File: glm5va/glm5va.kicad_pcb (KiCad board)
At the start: 2 copper layers, 21 parts, among them J1 BANK_xx1, J2 JIN, J3 POWER, U1 74HC245, U2 74HC245

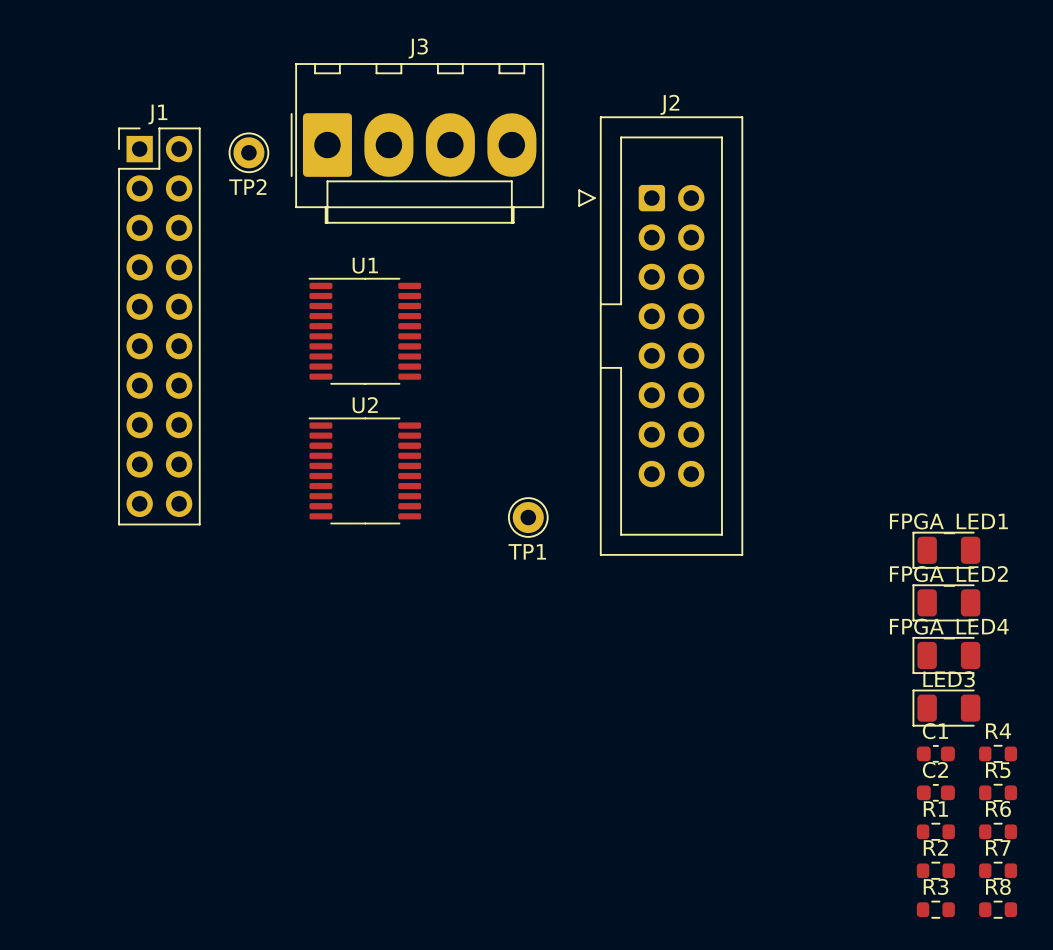
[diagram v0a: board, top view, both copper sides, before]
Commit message: glm5va: place components
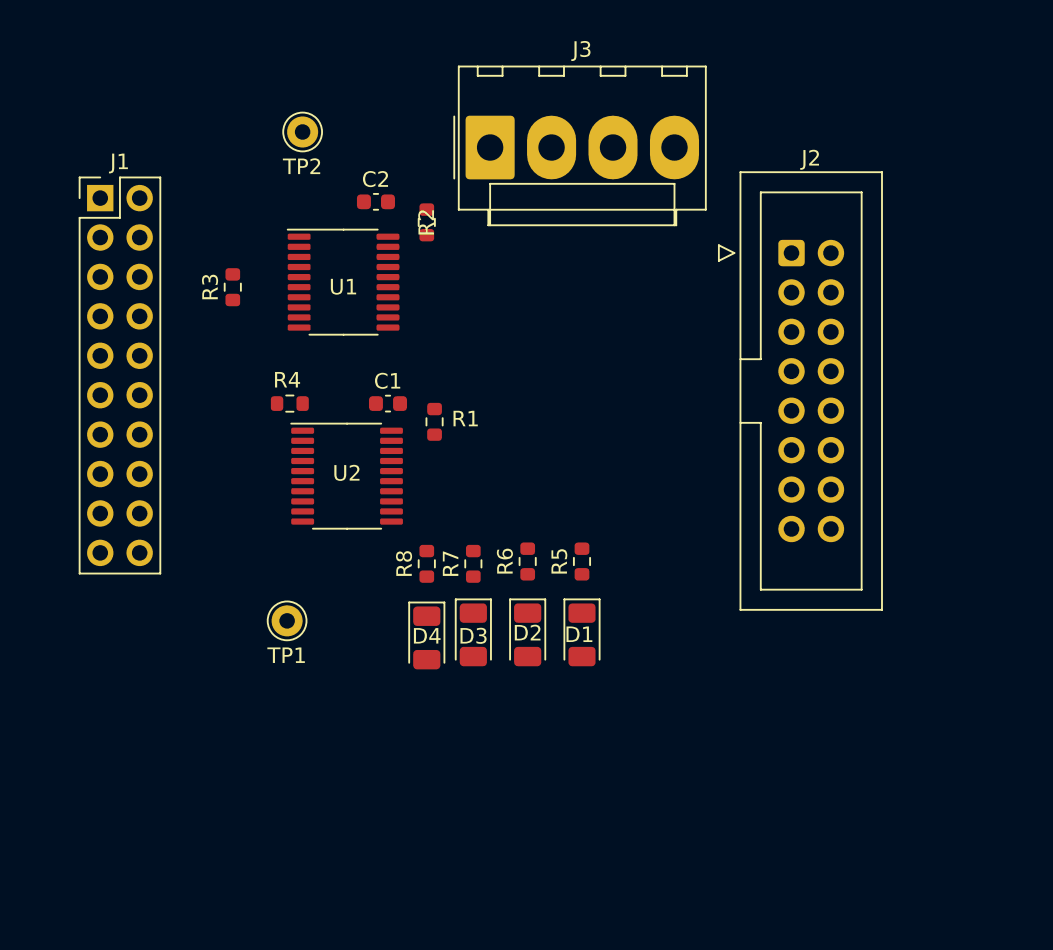
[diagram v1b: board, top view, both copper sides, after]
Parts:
- removed FPGA_LED1, FPGA_LED2, FPGA_LED4, LED3: 0603, LED_SMD:LED_1206_3216Metric
- added D1: 0603, LED_SMD:LED_1206_3216Metric, F.Cu at (151.0, 101.9)
- added D2: 0603, LED_SMD:LED_1206_3216Metric, F.Cu at (147.5, 101.9)
- added D3: 0603, LED_SMD:LED_1206_3216Metric, F.Cu at (144.0, 101.9)
- added D4: 0603, LED_SMD:LED_1206_3216Metric, F.Cu at (141.0, 102.1)
- R5, R6, R7, R8: value 2.2k/R0402 -> 2.2k
- moved R3 60.5 mm to (128.5, 79.5), turned to 90 degrees
- moved R2 53.1 mm to (141.0, 75.3), turned to 90 degrees
- moved C2 52.5 mm to (137.7, 74.0)
- moved R4 50.9 mm to (132.2, 87.0), turned to 180 degrees
- moved R8 43.0 mm to (141.0, 97.3), turned to 90 degrees
- moved C1 41.9 mm to (138.5, 87.0)
- moved R1 41.7 mm to (141.5, 88.2), turned to 90 degrees
- moved R7 39.2 mm to (144.0, 97.3), turned to 90 degrees
- moved R6 35.0 mm to (147.5, 97.2), turned to 90 degrees
- moved R5 30.7 mm to (151.0, 97.2), turned to 90 degrees
- moved TP1 16.9 mm to (132.0, 101.0)
- moved J3 10.5 mm to (145.1, 70.5)
- moved J2 9.67 mm to (164.5, 77.3)
- moved J1 4.05 mm to (120.0, 73.8)
- moved TP2 3.71 mm to (133.0, 69.5)
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
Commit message: glm5va: routing and layers ok
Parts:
- added G***: LOGO, LOGO, B.Cu at (136.0, 85.0)
- moved D4 11.2 mm to (151.0, 97.1)
- moved D3 11.1 mm to (154.0, 97.1)
- moved R7 11.0 mm to (154.0, 92.7)
- moved R8 11.0 mm to (151.0, 92.7)
- moved D2 10.6 mm to (157.0, 97.1)
- moved R6 10.5 mm to (157.0, 92.7)
- moved D1 10.2 mm to (160.0, 97.1)
- moved R5 10.1 mm to (160.0, 92.7)
- moved R3 7.66 mm to (133.8, 74.0), turned to 180 degrees
- moved J3 6.42 mm to (147.1, 76.6)
- moved TP2 5.41 mm to (128.5, 72.5)
- moved TP1 4.61 mm to (128.5, 98.0)
- moved J2 2.50 mm to (167.0, 76.9)
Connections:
- J1 pad 10: Net-(J1-Pin_10) -> /BANK_B5
- J1 pad 11: Net-(J1-Pin_11) -> /BANK_A4
- J1 pad 12: Net-(J1-Pin_12) -> /BANK_B4
- J1 pad 13: Net-(J1-Pin_13) -> /BANK_A3
- J1 pad 14: Net-(J1-Pin_14) -> /BANK_B3
- J1 pad 15: Net-(J1-Pin_15) -> /BANK_A2
- J1 pad 16: Net-(J1-Pin_16) -> /BANK_B2
- J1 pad 17: Net-(J1-Pin_17) -> /BANK_A1
- J1 pad 18: Net-(J1-Pin_18) -> /BANK_B1
- J1 pad 3: Net-(J1-Pin_3) -> /BANK_A8
- J1 pad 4: Net-(J1-Pin_4) -> /BANK_B8
- J1 pad 5: Net-(J1-Pin_5) -> /BANK_A7
- J1 pad 6: Net-(J1-Pin_6) -> /BANK_B7
- J1 pad 7: Net-(J1-Pin_7) -> /BANK_A6
- J1 pad 8: Net-(J1-Pin_8) -> /BANK_B6
- J1 pad 9: Net-(J1-Pin_9) -> /BANK_A5
- U1 pad 2: Net-(J1-Pin_17) -> /BANK_A8
- U1 pad 3: Net-(J1-Pin_15) -> /BANK_B8
- U1 pad 4: Net-(J1-Pin_13) -> /BANK_A7
- U1 pad 5: Net-(J1-Pin_11) -> /BANK_B7
- U1 pad 6: Net-(J1-Pin_9) -> /BANK_A6
- U1 pad 7: Net-(J1-Pin_7) -> /BANK_B6
- U1 pad 8: Net-(J1-Pin_5) -> /BANK_A5
- U1 pad 9: Net-(J1-Pin_3) -> /BANK_B5
- U2 pad 2: Net-(J1-Pin_18) -> /BANK_A4
- U2 pad 3: Net-(J1-Pin_16) -> /BANK_B4
- U2 pad 4: Net-(J1-Pin_14) -> /BANK_A3
- U2 pad 5: Net-(J1-Pin_12) -> /BANK_B3
- U2 pad 6: Net-(J1-Pin_10) -> /BANK_A2
- U2 pad 7: Net-(J1-Pin_8) -> /BANK_B2
- U2 pad 8: Net-(J1-Pin_6) -> /BANK_A1
- U2 pad 9: Net-(J1-Pin_4) -> /BANK_B1
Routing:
- net /B: track 0.00 -> 43.9 mm
- net /LAT: track 0.00 -> 40.2 mm
- net /G1: track 0.00 -> 37.8 mm, vias 0 -> 2
- net /G2: track 0.00 -> 34.7 mm, vias 0 -> 2
- net /OE: track 0.00 -> 33.7 mm
- net /CLK: track 0.00 -> 32.9 mm
- net /B2: track 0.00 -> 32.1 mm
- net /C: track 0.00 -> 32.1 mm
- net /R2: track 0.00 -> 31.5 mm
- net /A: track 0.00 -> 31.3 mm
- net /R1: track 0.00 -> 29.9 mm
- net /B1: track 0.00 -> 29.0 mm
- net Net-(U2-B1): track 0.00 -> 21.9 mm, vias 0 -> 2
- net Net-(U2-B3): track 0.00 -> 18.9 mm, vias 0 -> 2
- net Net-(U2-B7): track 0.00 -> 16.4 mm
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- added copper zone on F.Cu, net +5V
- added copper zone on B.Cu, net GND
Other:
- board outline added: 57.5 x 32 mm
- board text added: "glm5va v1.0"
